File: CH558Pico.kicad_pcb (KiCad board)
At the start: 2 copper layers, 21 x 50.8 mm, 18 parts, among them CN1 CON_USB-C-16, J1 Conn_01x20, J2 Conn_01x20, Q1 TR_NMOS_IRLML6344, SW1 SW_Push, SW2 SW_Push, U1 MCU_CH559L

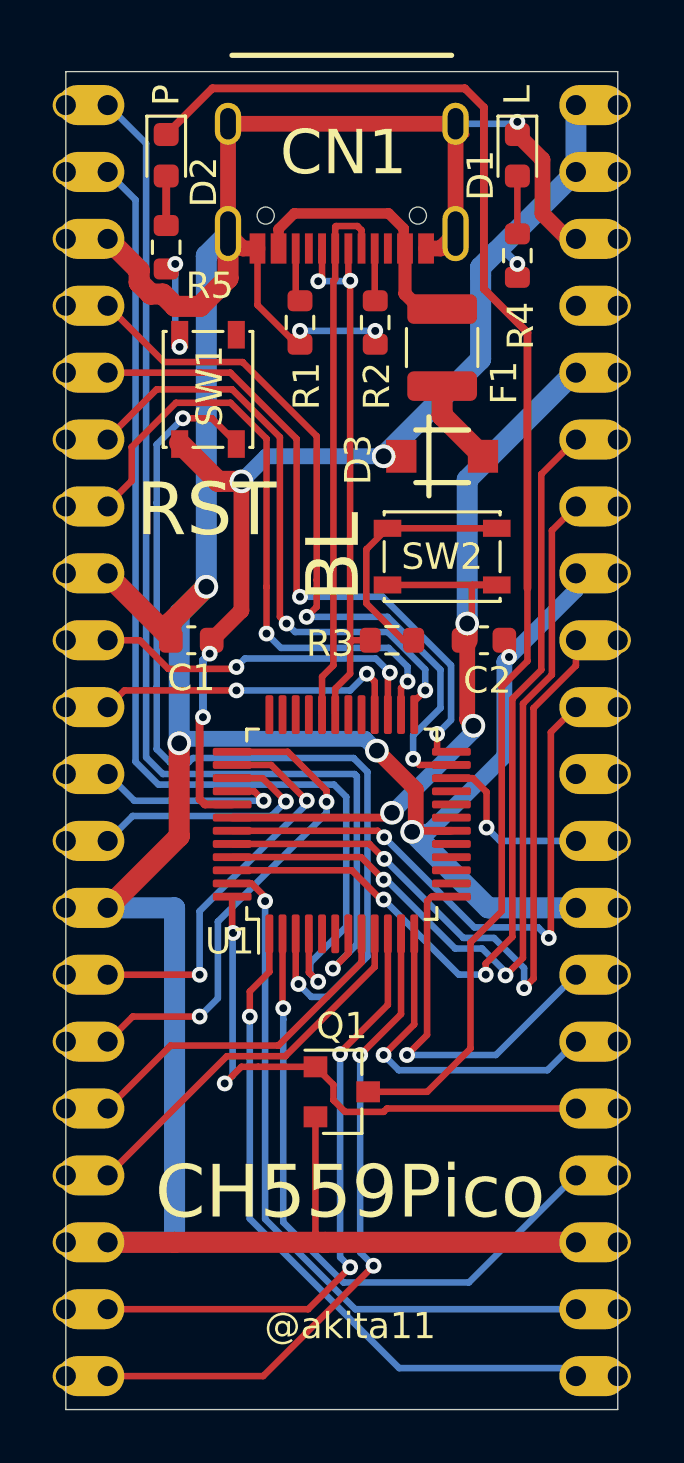
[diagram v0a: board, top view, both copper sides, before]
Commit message: BLピン・シルクの修正
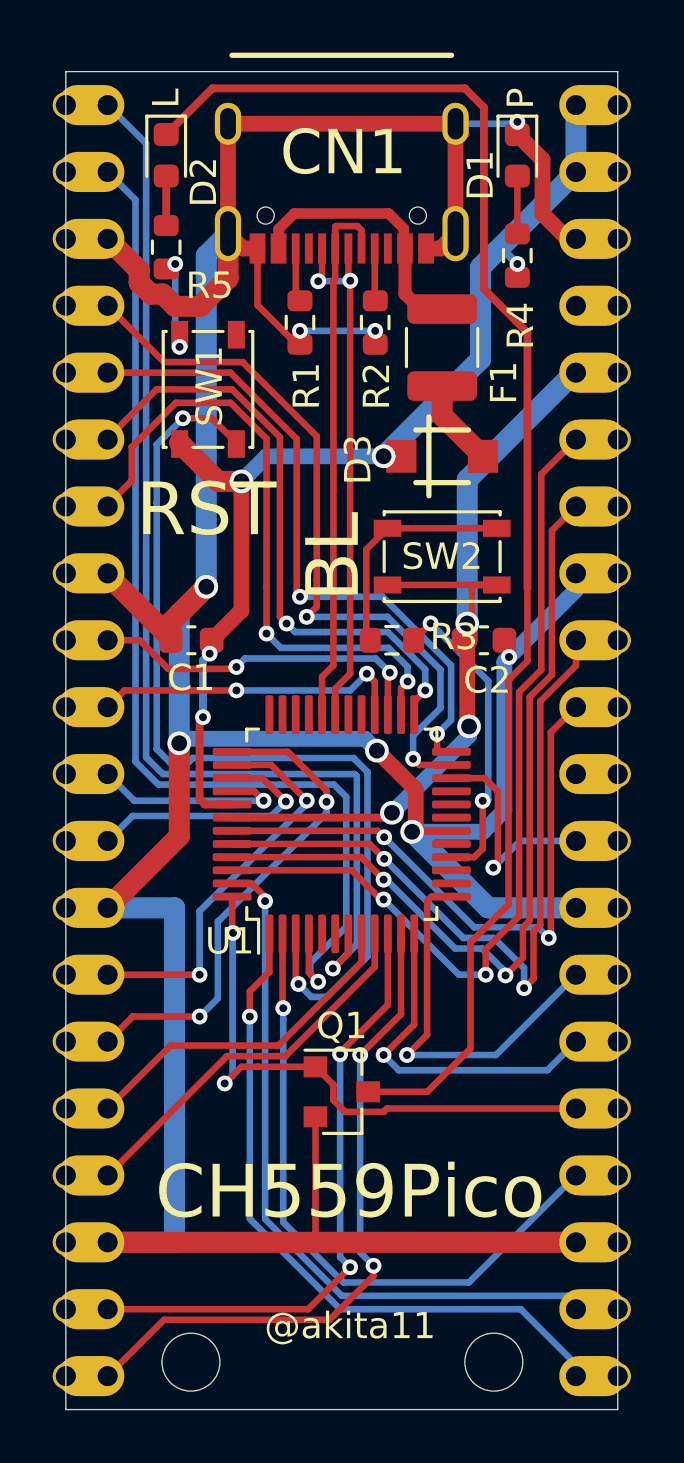
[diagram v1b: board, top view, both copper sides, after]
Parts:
- added REF**: MountingHole_2.2mm_M2, MountingHole:MountingHole_2.2mm_M2, F.Cu at (16.2, 49.0)
- added REF**: MountingHole_2.2mm_M2, MountingHole:MountingHole_2.2mm_M2, F.Cu at (4.75, 49.0)
- turned R3 to 0 degrees
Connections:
- CN1 pad A8: Net-(CN1-PadA8) -> unconnected-(CN1-PadA8)
- CN1 pad B8: Net-(CN1-PadB8) -> unconnected-(CN1-PadB8)
- J2 pad 10: Net-(J2-Pad10) -> unconnected-(J2-Pad10)
- J2 pad 17: Net-(J2-Pad17) -> unconnected-(J2-Pad17)
- R3 pad 2: /UDP -> /P4.6
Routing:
- net /P4.6: track 0.00 -> 11.9 mm, vias 0 -> 2
- net /P2.1: track 6.57 -> 8.57 mm
- net GND: track 152.9 -> 154.1 mm
- net Net-(R3-Pad1): track 9.71 -> 8.79 mm
- net /UDP: track 21.1 -> 20.4 mm
- net /P1.6: track 26.0 -> 26.6 mm
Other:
- net class Default removed
- board text added: "A1.0"
- board text added: "A1.1"
- board text added: "A1.2~"
- board text added: "A1.3"
- board text added: "A1.4"
- board text added: "A1.5"
- board text added: "A1.6"
- board text added: "A1.7"
- board text added: "~2.4"
- board text added: "~2.5"
- board text removed: "1.0"
- board text removed: "1.1"
- board text removed: "1.2"
- board text removed: "1.3"
- board text removed: "1.4"
- board text removed: "1.5"
- board text removed: "1.6"
- board text removed: "1.7"
- board text removed: "2.4"
- board text removed: "2.5"
